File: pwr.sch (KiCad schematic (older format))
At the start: 22 parts, among them U1 FT601

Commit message: Cloack, LMS are added
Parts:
- added C26: C, Capacitors_SMD:C_0603_HandSoldering, symbol C
- added R4, R5, R6, R7: 4.7k, Resistors_SMD:R_0603_HandSoldering, symbol R
- added TP1: ~INIT, Measurement_Points:Measurement_Point_Square-SMD-Pad_Big, symbol TEST
- added TP2: DONE, Measurement_Points:Measurement_Point_Square-SMD-Pad_Big, symbol TEST
- added TP3: ~PRG, Measurement_Points:Measurement_Point_Square-SMD-Pad_Big, symbol TEST
- added U4: ECP5, sdr-foots:ECP5_381, symbol ECP5-RESCUE-sdr
- added X2: CONN_01X10, Pin_Headers:Pin_Header_Angled_1x10_Pitch2.00mm, symbol CONN_01X10
- C1, C10, C11, C12, C13, C14, C15, C16, C17, C18, C19, C2, C20, C3, C4, C5, C6, C7, C8, C9: renamed from C?; footprint (none) -> Capacitors_SMD:C_0603_HandSoldering
- R1: renamed from R?; footprint (none) -> Resistors_SMD:R_0603_HandSoldering
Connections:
- net labels added: +1V1, CFG_MCLK, CFG_MISO, CFG_MOSI, DONE, TCK, TDI, TDO, TMS, ~CFG_CS, ~CFG_HOLD, ~INIT, ~PRG
- wire segments 55 -> 97
- no-connect marks 0 -> 1
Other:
- note added: "SPI SLAVE"

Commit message: Schematic is done except RF.
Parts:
- removed unit 2 of U4
- removed unit 1 of U4
- added C72, C73: 4.7u, Capacitors_SMD:C_0402, symbol C
- added C74, C75: 10u, Capacitors_SMD:C_0402, symbol C
- added C76, C77: 100p, Capacitors_SMD:C_0402, symbol C
- added C78, C79, C80, C81, C82, C83, C84, C85: 1u, Capacitors_SMD:C_0402, symbol C
- added L4, L5: 4.7u, Inductors:Inductor_Taiyo-Yuden_MD-4040, symbol L
- added R22: 120k 1%, Resistors_SMD:R_0402, symbol R
- added R23: 100k 1%, Resistors_SMD:R_0402, symbol R
- added R24: 84.5k 1%, Resistors_SMD:R_0402, symbol R
- added R25: 560k 1%, Resistors_SMD:R_0402, symbol R
- added U10, U8, U9: MIC94310, sdr-foots:DFN-4, symbol MIC94310
- added U6: PAM2306, Housings_DFN_QFN:DFN-12-1EP_3x3mm_Pitch0.45mm, symbol PAM2306
- added U7: NCP186, sdr-foots:DFN-8-1EP_1.6x1.2mm_Pitch0.4mm, symbol NCP186
- C1, C11, C12, C13, C17, C19, C2, C3, C4, C9: footprint Capacitors_SMD:C_0603_HandSoldering -> Capacitors_SMD:C_0402
- C10, C14, C15, C16, C18, C20, C5, C6, C7, C8: value 0.1u -> 100n; footprint Capacitors_SMD:C_0603_HandSoldering -> Capacitors_SMD:C_0402
- C26: value C -> 100n; footprint Capacitors_SMD:C_0603_HandSoldering -> Capacitors_SMD:C_0402
- R1, R4, R5, R6, R7: footprint Resistors_SMD:R_0603_HandSoldering -> Resistors_SMD:R_0402
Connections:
- net labels added: +1V8, +5V, 5V_RPi, LMS_A1V8, LMS_A2V5, LMS_A3V3, LMS_D1V8, LMS_D3V3, LMS_IO
- wire segments 97 -> 166
- no-connect marks 1 -> 2
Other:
- note added: "Voltage should be tuned 100mV more\nthan 3V3 to let 3V3 analog LDO work\nproperly. All components which require\n3V3 are able to work with 3V4 as well."
- moved on the sheet: C10, C11, C12, C13, C14, C15, C16, C17, C18, C19, C2, C20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

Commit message: Placed most components for FTDI. Begin tracing FT601
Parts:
- removed C26: 100n, Capacitors_SMD:C_0402, symbol C
- removed TP1: ~INIT, Measurement_Points:Measurement_Point_Square-SMD-Pad_Big, symbol TEST
- removed TP2: DONE, Measurement_Points:Measurement_Point_Square-SMD-Pad_Big, symbol TEST
- removed TP3: ~PRG, Measurement_Points:Measurement_Point_Square-SMD-Pad_Big, symbol TEST
- removed X2: CONN_01X10, Pin_Headers:Pin_Header_Angled_1x10_Pitch2.00mm, symbol CONN_01X10
- added X2: CONN_01X08, Pin_Headers:Pin_Header_Straight_1x08_Pitch1.27mm, symbol CONN_01X08
- C1, C10, C11, C12, C13, C14, C15, C18, C19, C2, C20, C4, C5, C76, C77, C78, C79, C8, C80, C81, C82, C83, C84, C85: footprint Capacitors_SMD:C_0402 -> Capacitors_SMD:C_0603
- C16, C6, C7: value 100n -> C; footprint Capacitors_SMD:C_0402 -> Capacitors_SMD:C_0603
- C17, C3, C9: value 0.47u -> C; footprint Capacitors_SMD:C_0402 -> Capacitors_SMD:C_0603
- C72: value 4.7u -> 10u; footprint Capacitors_SMD:C_0402 -> Capacitors_SMD:C_0805
- C73: value 4.7u -> C; footprint Capacitors_SMD:C_0402 -> Capacitors_SMD:C_0603
- C74, C75: footprint Capacitors_SMD:C_0402 -> Capacitors_SMD:C_0805
- R1, R22, R23, R24, R25, R4, R5, R6, R7: footprint Resistors_SMD:R_0402 -> Resistors_SMD:R_0603
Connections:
- wire segments 166 -> 159
- no-connect marks 2 -> 1
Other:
- note removed: "Near pin VCC33(20)"
- moved on the sheet: C10, C13, C18, R4, R5

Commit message: Right before Sitch power retracing
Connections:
- net +3V3: now also R7.2; no longer R6.2
- net GNDD: now also R6.1, X2.4 (P4); no longer R7.2, X2.5 (P5)
- net TCK: now also R6.2, X2.3 (P3); no longer R7.1, X2.6 (P6)
- net TDI: now also R4.2, X2.1 (P1); no longer R5.1, X2.2 (P2)
- net TDO: now also R7.1, X2.5 (P5); no longer R4.2, X2.1 (P1)
- net TMS: now also R5.1, X2.2 (P2); no longer R6.1, X2.4 (P4)
- net ~INIT: now also X2.6 (P6); no longer X2.8 (P8)
- net ~PRG: now also X2.8 (P8); no longer X2.3 (P3)
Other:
- moved on the sheet: R6, R7
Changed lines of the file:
@@
 LIBS:sdr
 LIBS:usb-type-c
+LIBS:sdr-cache
 EELAYER 25 0
 EELAYER END
@@
 L R R7
 U 1 1 589EF8BF
-P 6600 1650
-F 0 "R7" V 6680 1650 50  0000 C CNN
-F 1 "4.7k" V 6600 1650 50  0000 C CNN
-F 2 "Resistors_SMD:R_0603" V 6530 1650 50  0001 C CNN
-F 3 "" H 6600 1650 50  0000 C CNN
-	1    6600 1650
+P 6600 1550
+F 0 "R7" V 6680 1550 50  0000 C CNN
+F 1 "4.7k" V 6600 1550 50  0000 C CNN
+F 2 "Resistors_SMD:R_0603" V 6530 1550 50  0001 C CNN
+F 3 "" H 6600 1550 50  0000 C CNN
+	1    6600 1550
 	0    1    1    0
 $EndComp
@@
 L GNDD #PWR013
 U 1 1 589F005F
-P 6300 1900
-F 0 "#PWR013" H 6300 1650 50  0001 C CNN
-F 1 "GNDD" H 6300 1750 50  0000 C CNN
-F 2 "" H 6300 1900 50  0000 C CNN
-F 3 "" H 6300 1900 50  0000 C CNN
-	1    6300 1900
+P 6200 1800
+F 0 "#PWR013" H 6200 1550 50  0001 C CNN
+F 1 "GNDD" H 6200 1650 50  0000 C CNN
+F 2 "" H 6200 1800 50  0000 C CNN
+F 3 "" H 6200 1800 50  0000 C CNN
+	1    6200 1800
 	1    0    0    -1
 $EndComp
@@
 Text Label 9950 1150 0    60   ~ 0
 TCK
+Text Label 6850 1550 0    60   ~ 0
+TDO
 Text Label 6850 1150 0    60   ~ 0
-TDO
-Text Label 6850 1250 0    60   ~ 0
 TDI
-Text Label 6850 1350 0    60   ~ 0
+Text Label 6850 1850 0    60   ~ 0
 ~PRG
 Text Label 9900 1700 0    60   ~ 0
@@
 Text Label 6850 1750 0    60   ~ 0
 DONE
-Text Label 6850 1850 0    60   ~ 0
+Text Label 6850 1650 0    60   ~ 0
 ~INIT
-Text Label 6850 1650 0    60   ~ 0
+Text Label 6850 1350 0    60   ~ 0
 TCK
-Text Label 6850 1450 0    60   ~ 0
+Text Label 6850 1250 0    60   ~ 0
 TMS
 $Comp
@@
 L R R6
 U 1 1 589F2A11
-P 6600 1450
-F 0 "R6" V 6680 1450 50  0000 C CNN
-F 1 "4.7k" V 6600 1450 50  0000 C CNN
-F 2 "Resistors_SMD:R_0603" V 6530 1450 50  0001 C CNN
-F 3 "" H 6600 1450 50  0000 C CNN
-	1    6600 1450
-	0    1    1    0
+P 6200 1550
+F 0 "R6" V 6280 1550 50  0000 C CNN
+F 1 "4.7k" V 6200 1550 50  0000 C CNN
+F 2 "Resistors_SMD:R_0603" V 6130 1550 50  0001 C CNN
+F 3 "" H 6200 1550 50  0000 C CNN
+	1    6200 1550
+	-1   0    0    1
 $EndComp
 Text Notes 10000 2850 0    60   ~ 0
@@
 	9850 1250 9950 1250
 Wire Wire Line
-	6750 1650 7100 1650
-Wire Wire Line
 	7100 1750 6850 1750
 Wire Wire Line
 	6850 1850 7100 1850
-Wire Wire Line
-	6300 1550 7100 1550
-Wire Wire Line
-	6750 1450 7100 1450
-Wire Wire Line
-	6750 1150 7100 1150
-Wire Wire Line
-	6750 1250 7100 1250
-Wire Wire Line
-	7100 1350 6850 1350
 Wire Wire Line
 	8650 1550 8650 2850
@@
 	1    0    0    -1
 $EndComp
-Connection ~ 6300 1150
-Wire Wire Line
-	6450 1150 6300 1150
-Connection ~ 6300 1250
-Wire Wire Line
-	6450 1250 6300 1250
-Wire Wire Line
-	6300 1450 6450 1450
-Wire Wire Line
-	6300 900  6300 1450
-Wire Wire Line
-	6300 1900 6300 1550
-Wire Wire Line
-	6450 1650 6300 1650
-Connection ~ 6300 1650
-$Comp
-L +3V3 #PWR?
+$Comp
+L +3V3 #PWR036
 U 1 1 58AEBAC7
-P 6300 900
-F 0 "#PWR?" H 6300 750 50  0001 C CNN
-F 1 "+3V3" H 6300 1040 50  0000 C CNN
-F 2 "" H 6300 900 50  0000 C CNN
-F 3 "" H 6300 900 50  0000 C CNN
-	1    6300 900
-	1    0    0    -1
-$EndComp
+P 6400 950
+F 0 "#PWR036" H 6400 800 50  0001 C CNN
+F 1 "+3V3" H 6400 1090 50  0000 C CNN
+F 2 "" H 6400 950 50  0000 C CNN
+F 3 "" H 6400 950 50  0000 C CNN
+	1    6400 950
+	1    0    0    -1
+$EndComp
+Wire Wire Line
+	6750 1150 7100 1150
+Wire Wire Line
+	6750 1250 7100 1250
+Wire Wire Line
+	6750 1550 7100 1550
+Wire Wire Line
+	7100 1650 6850 1650
+Wire Wire Line
+	6400 950  6400 1550
+Wire Wire Line
+	6400 1550 6450 1550
+Wire Wire Line
+	6450 1250 6400 1250
+Connection ~ 6400 1250
+Wire Wire Line
+	6450 1150 6400 1150
+Connection ~ 6400 1150
+Wire Wire Line
+	6200 1350 7100 1350
+Wire Wire Line
+	6200 1400 6200 1350
+Wire Wire Line
+	7100 1450 6300 1450
+Wire Wire Line
+	6300 1450 6300 1750
+Wire Wire Line
+	6200 1700 6200 1800
+Wire Wire Line
+	6300 1750 6200 1750
+Connection ~ 6200 1750
 $EndSCHEMATC

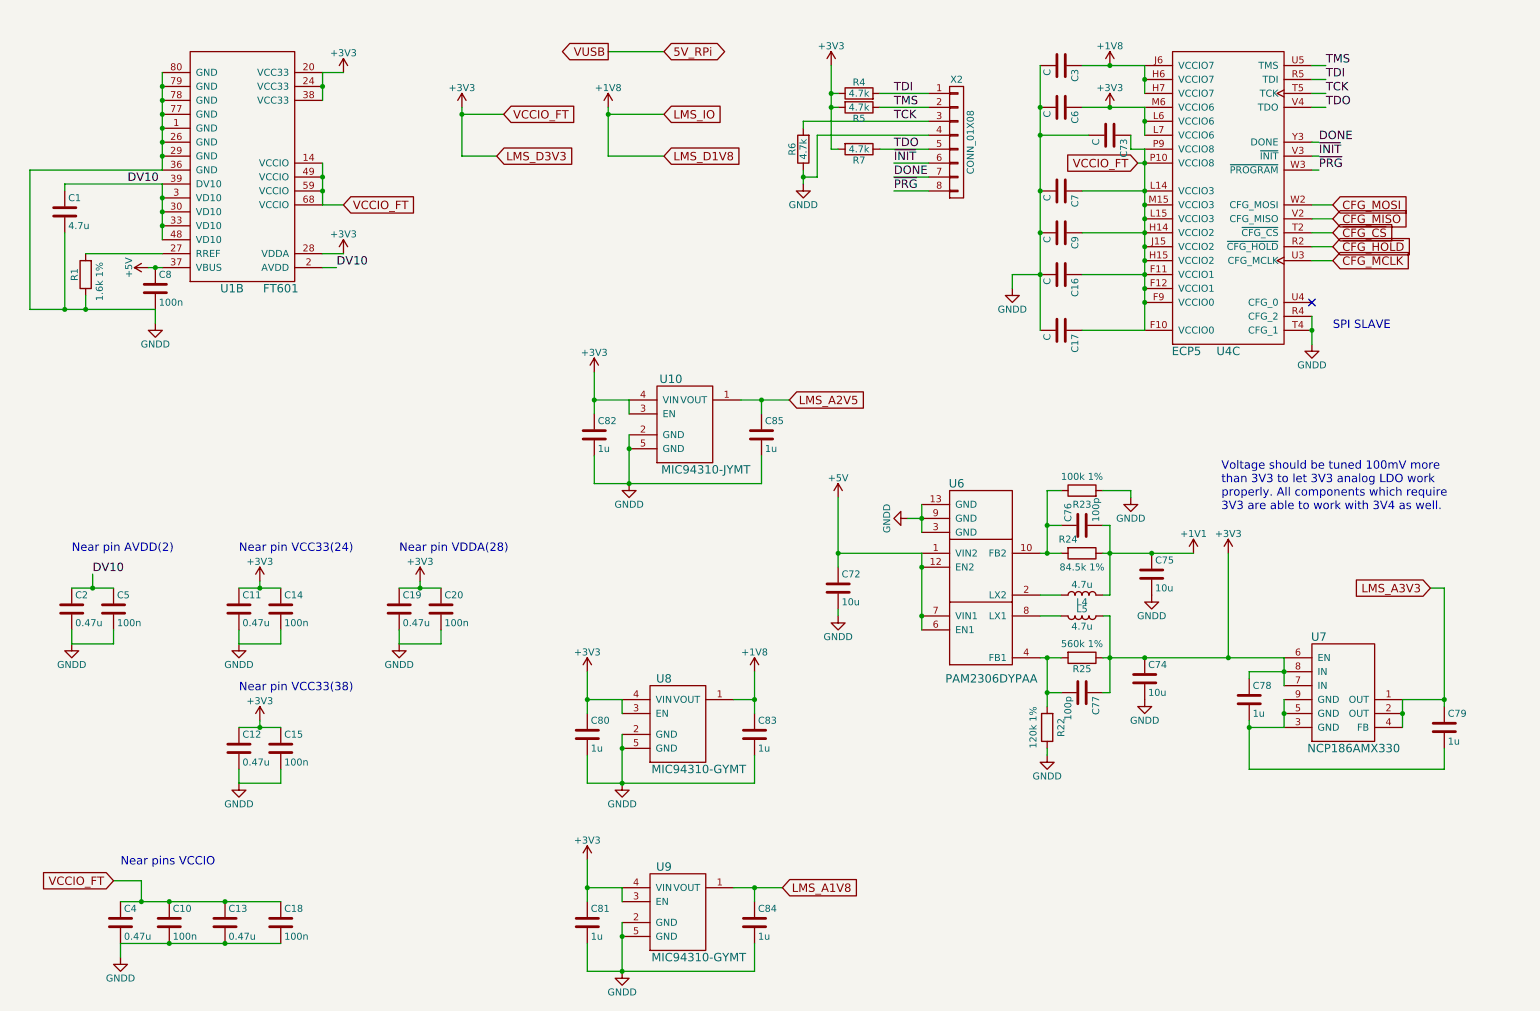
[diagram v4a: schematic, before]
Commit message: Power is traced. Placing capacitors for FPGA
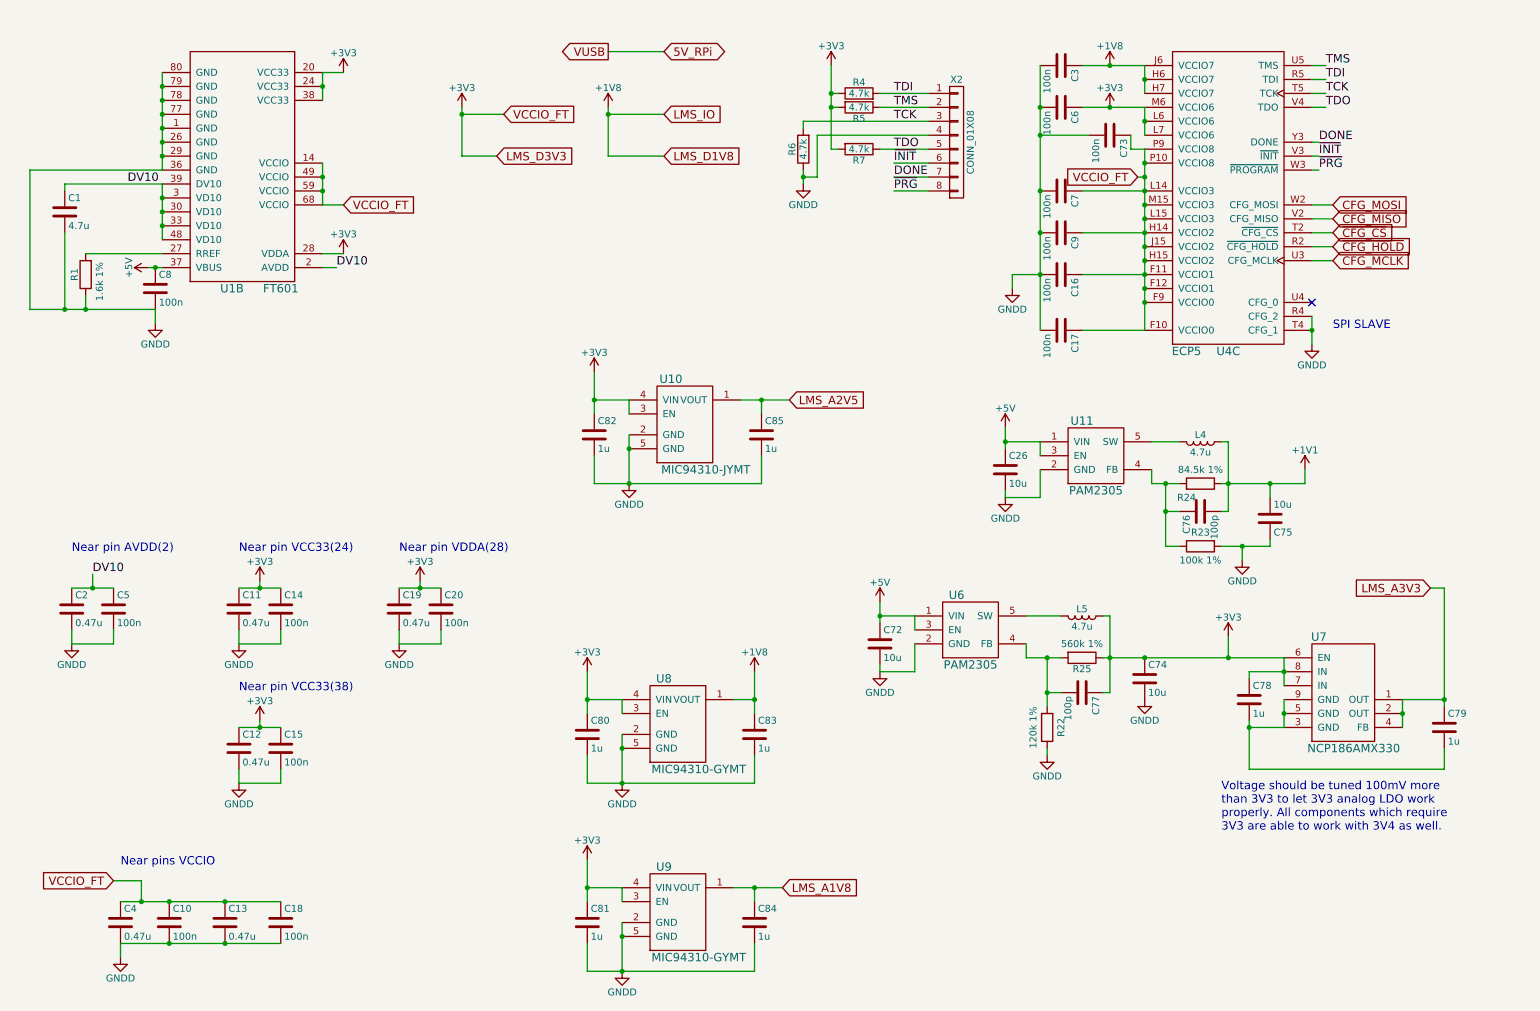
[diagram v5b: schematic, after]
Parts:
- removed U6: PAM2306, Housings_DFN_QFN:DFN-12-1EP_3x3mm_Pitch0.45mm, symbol PAM2306
- added C26: 10u, Capacitors_SMD:C_0805, symbol C
- added U11, U6: PAM2305, TO_SOT_Packages_SMD:SOT-23-5, symbol PAM2305
- C16, C17, C3, C6, C7, C73, C9: value C -> 100n
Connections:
- net +1V1: now also C75.2; no longer C75.1
- net +5V: now also C26.1, U11.1 (VIN), U11.3 (EN), U6.1 (VIN), U6.3 (EN)
- net GNDD: now also C75.1, C26.2, U11.2 (GND), U6.2 (GND); no longer C75.2
- net at C76.1, R23.1, R24.2: now also U11.4 (FB)
- net at L4.1: now also U11.5 (SW)
- net at C77.2, R22.2, R25.2: now also U6.4 (FB)
- net at L5.2: now also U6.5 (SW)
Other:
- moved on the sheet: C72, C75, C76, L4, R23, R24

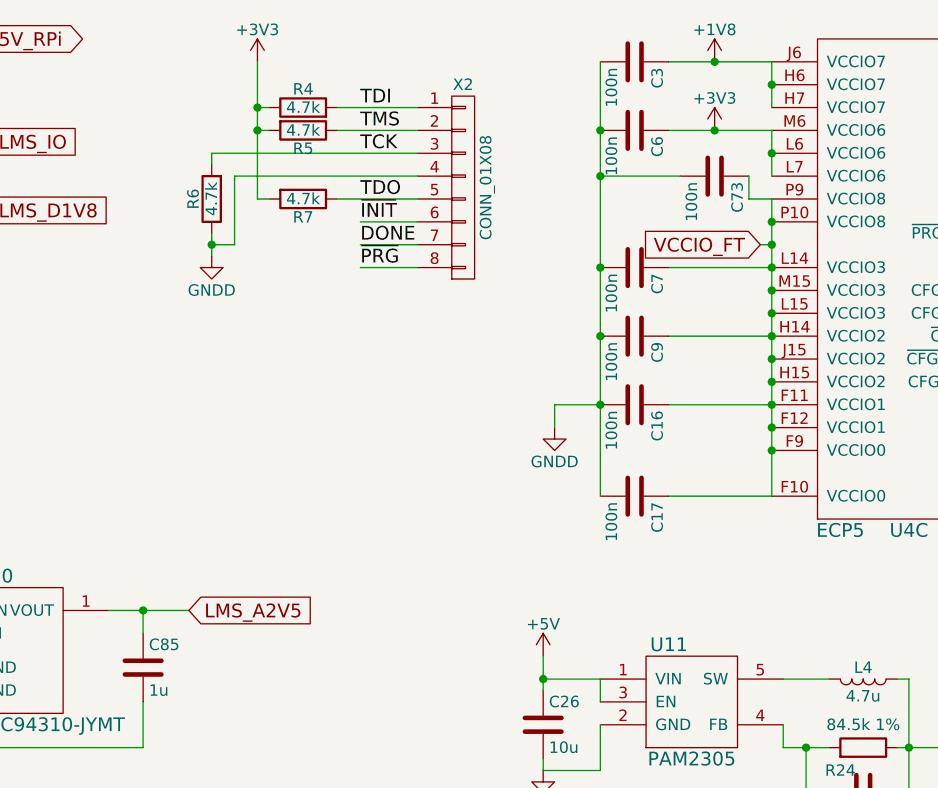
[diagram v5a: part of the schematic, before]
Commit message: Caps for FPGA are placed. Most of FPGA power is traced. Need to trace Rpi connector
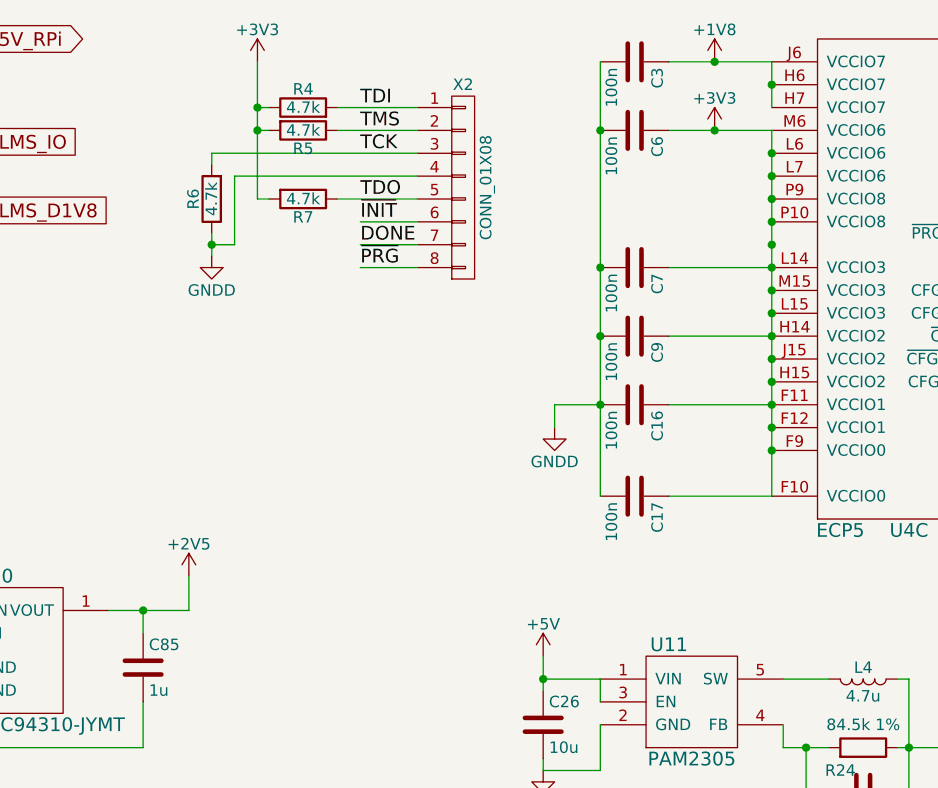
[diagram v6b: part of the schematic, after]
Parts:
- removed C73: 100n, Capacitors_SMD:C_0603, symbol C
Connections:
- net LMS_A2V5 renamed +2V5
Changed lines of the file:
@@
 Text Notes 10000 2850 0    60   ~ 0
 SPI SLAVE
-Text GLabel 8600 1750 0    60   Input ~ 0
-VCCIO_FT
 Text GLabel 4050 1300 2    60   Input ~ 0
 VCCIO_FT
@@
 	6850 1850 7100 1850
 Wire Wire Line
-	8650 1550 8650 2850
+	8650 1250 8650 2850
 Wire Wire Line
 	4050 1300 3750 1300
@@
 $EndComp
 Connection ~ 4700 3350
-Text GLabel 6100 3350 2    60   Input ~ 0
-LMS_A2V5
 Connection ~ 5900 3350
 Wire Wire Line
@@
 	1    0    0    -1
 $EndComp
-Wire Wire Line
-	8650 1250 8650 1450
 Connection ~ 8650 1350
 Wire Wire Line
@@
 	7700 2450 7700 2550
 $Comp
-L C C73
-U 1 1 58AD9C04
-P 8400 1450
-F 0 "C73" H 8425 1550 50  0000 L CNN
-F 1 "100n" H 8425 1350 50  0000 L CNN
-F 2 "Capacitors_SMD:C_0603" H 8438 1300 50  0001 C CNN
-F 3 "" H 8400 1450 50  0000 C CNN
-	1    8400 1450
-	0    1    1    0
-$EndComp
-Wire Wire Line
-	8550 1450 8550 1550
-Wire Wire Line
-	8550 1550 8650 1550
-Wire Wire Line
-	8250 1450 7900 1450
-Connection ~ 7900 1450
-$Comp
 L CONN_01X08 X2
 U 1 1 58AE8617
@@
 Wire Wire Line
 	7900 3850 7900 4050
-Wire Wire Line
-	8600 1750 8650 1750
 Connection ~ 8650 1750
 Connection ~ 8650 1650
+Connection ~ 8650 1450
+Connection ~ 8650 1550
+$Comp
+L +2V5 #PWR037
+U 1 1 58BCAEE2
+P 6100 3200
+F 0 "#PWR037" H 6100 3050 50  0001 C CNN
+F 1 "+2V5" H 6100 3340 50  0000 C CNN
+F 2 "" H 6100 3200 50  0000 C CNN
+F 3 "" H 6100 3200 50  0000 C CNN
+	1    6100 3200
+	1    0    0    -1
+$EndComp
+Wire Wire Line
+	6100 3350 6100 3200
 $EndSCHEMATC
